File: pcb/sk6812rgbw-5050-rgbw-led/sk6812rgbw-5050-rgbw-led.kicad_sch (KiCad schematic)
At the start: 0 parts

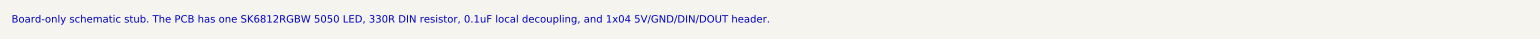
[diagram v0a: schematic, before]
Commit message: Redraw addressable LED carrier boards
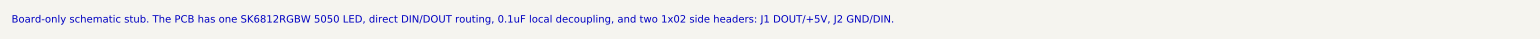
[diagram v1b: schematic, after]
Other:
- note added: "Board-only schematic stub. The PCB has one SK6812RGBW 5050 LED, direct DIN/DOUT routing, 0.1uF local decoupling, and two 1x02 side headers: J1 DOUT/+5V, J2 GND/DIN."
- note removed: "Board-only schematic stub. The PCB has one SK6812RGBW 5050 LED, 330R DIN resistor, 0.1uF local decoupling, and 1x04 5V/GND/DIN/DOUT header."
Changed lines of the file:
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@@
 	(generator_version "1.0")
 	(paper "A4")
-	(text "Board-only schematic stub. The PCB has one SK6812RGBW 5050 LED, 330R DIN resistor, 0.1uF local decoupling, and 1x04 5V/GND/DIN/DOUT header." (at 65 76.2 0)
+	(text "Board-only schematic stub. The PCB has one SK6812RGBW 5050 LED, direct DIN/DOUT routing, 0.1uF local decoupling, and two 1x02 side headers: J1 DOUT/+5V, J2 GND/DIN." (at 65 76.2 0)
 		(effects (font (size 1.27 1.27)) (justify left bottom))
 	)

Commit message: Clean addressable LED carrier routing
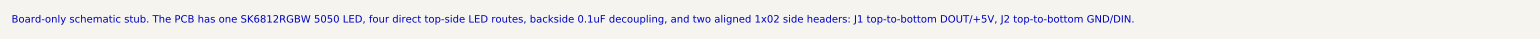
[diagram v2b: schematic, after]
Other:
- note added: "Board-only schematic stub. The PCB has one SK6812RGBW 5050 LED, four direct top-side LED routes, backside 0.1uF decoupling, and two aligned 1x02 side headers: J1 top-to-bottom DOUT/+5V, J2 top-to-bottom GND/DIN."
- note removed: "Board-only schematic stub. The PCB has one SK6812RGBW 5050 LED, direct DIN/DOUT routing, 0.1uF local decoupling, and two 1x02 side headers: J1 DOUT/+5V, J2 GND/DIN."
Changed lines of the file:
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@@
 	(generator_version "1.0")
 	(paper "A4")
-	(text "Board-only schematic stub. The PCB has one SK6812RGBW 5050 LED, direct DIN/DOUT routing, 0.1uF local decoupling, and two 1x02 side headers: J1 DOUT/+5V, J2 GND/DIN." (at 65 76.2 0)
+	(text "Board-only schematic stub. The PCB has one SK6812RGBW 5050 LED, four direct top-side LED routes, backside 0.1uF decoupling, and two aligned 1x02 side headers: J1 top-to-bottom DOUT/+5V, J2 top-to-bottom GND/DIN." (at 65 76.2 0)
 		(effects (font (size 1.27 1.27)) (justify left bottom))
 	)
